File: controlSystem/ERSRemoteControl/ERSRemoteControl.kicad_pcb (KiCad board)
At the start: 2 copper layers, 58.8 x 37.7 mm, 60 parts, among them J1 USB_C_Receptacle_USB2.0_14P, J2 0022-232041, J5 0022-232021, J6 0022-232021, J7 0022-232031, SW1 SW_SPDT, SW2 SW_Push, SW3 SW_Push, SW4 SW_Push, SW5 SW_Push, SW6 SW_Push, SW7 SW_Push, U1 TPS63070, U2 ESP32-S3-WROOM-1

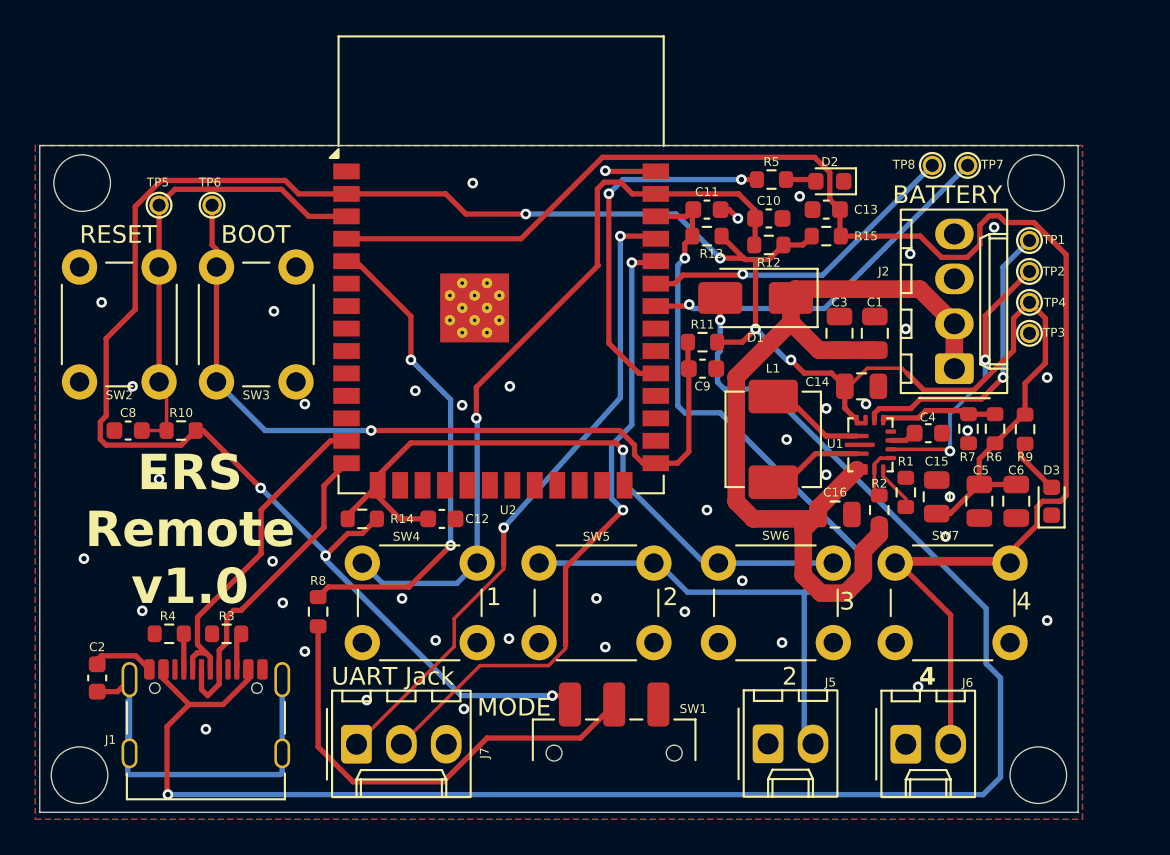
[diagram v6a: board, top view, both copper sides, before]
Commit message: Removed mode switch cleaned up traces, minimum trace size to .3 mm
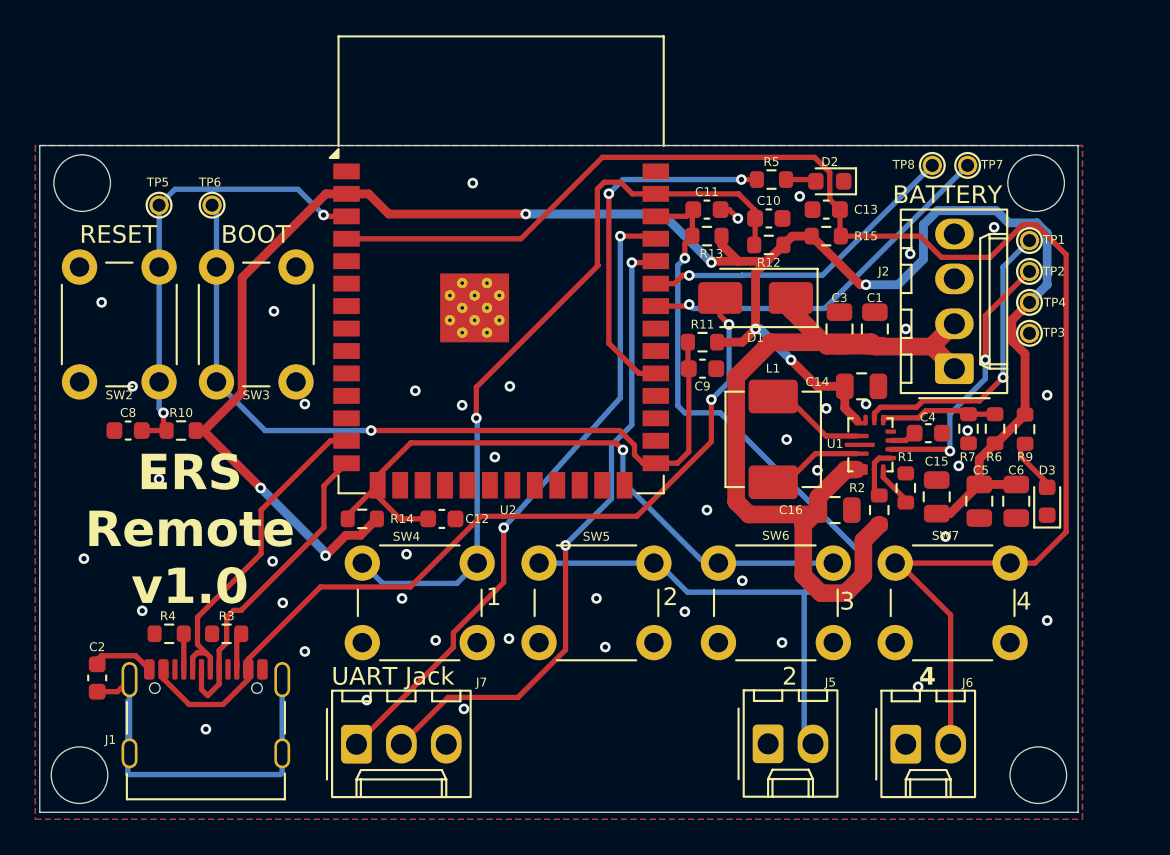
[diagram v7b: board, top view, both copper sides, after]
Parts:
- removed R8: 220, Resistor_SMD:R_0603_1608Metric
- removed SW1: SW_SPDT, Button_Switch_SMD:SW_SPDT_CK_JS102011SAQN
- moved C1 0.25 mm to (121.2, 101.2)
- moved C16 0.25 mm to (119.0, 111.5)
- moved C3 0.25 mm to (119.2, 101.2)
- moved D3 0.25 mm to (131.0, 111.0)
- moved R1 0.25 mm to (123.0, 110.2)
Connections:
- U2 pad 5: Net-(U2-IO5) -> unconnected-(U2-IO5-Pad5)
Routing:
- net +5V: track 95.9 -> 47.7 mm
- net Net-(U2-IO5): track 27.5 -> 0.00 mm, vias 2 -> 0
- net Net-(SW1-B): track 26.3 -> 0.00 mm
- net +3.3V: track 141.7 -> 117.1 mm
- net /SWITCH 4: track 92.9 -> 86.2 mm
- net GND: track 8.53 -> 5.66 mm, vias 42 -> 43
- net Net-(D1-K): track 51.0 -> 49.1 mm
- net /RESET: track 26.9 -> 25.9 mm, vias 0 -> 2
- net unconnected-(U2-IO5-Pad5): track 0.00 -> 0.53 mm
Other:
- board text removed: "MODE"

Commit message: Fixed traces, removed the mode switch and added debouncing logic
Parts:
- moved R15 0.25 mm to (118.5, 96.2)
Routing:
- net /SWITCH 4: track 86.2 -> 72.5 mm, vias 0 -> 3
- net GND: vias 43 -> 47
